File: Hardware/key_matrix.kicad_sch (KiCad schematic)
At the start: 80 parts, among them SW1 ESC, SW10 TAB, SW11 Q, SW12 W, SW13 E, SW14 R, SW15 T, SW16 NA, SW17 M1, SW18 CAPS, SW19 A, SW2 `, SW20 S, SW21 D, SW22 F, SW23 G, SW24 NA, SW25 M2, SW26 M3, SW28 SHIFT, SW29 CTRL, SW3 1, SW31 Z, SW32 WIN, SW34 X, SW35 FN, SW37 C, SW38 ALT, SW4 2, SW40 V, SW41 SPACE, SW43 B, SW44 DEL, SW46 NA, SW47 NA, SW5 3, SW6 4, SW7 5, SW8 6, SW9 M0

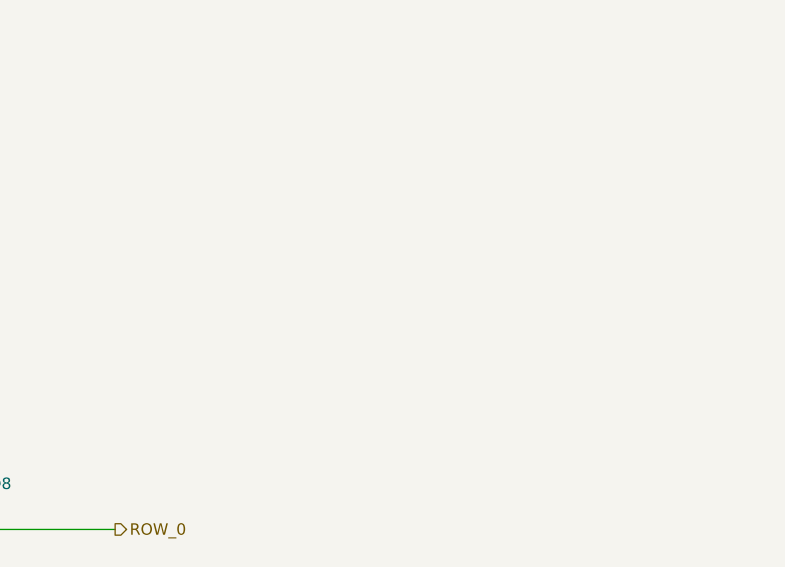
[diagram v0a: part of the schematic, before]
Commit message: added rotary encoder to schematic
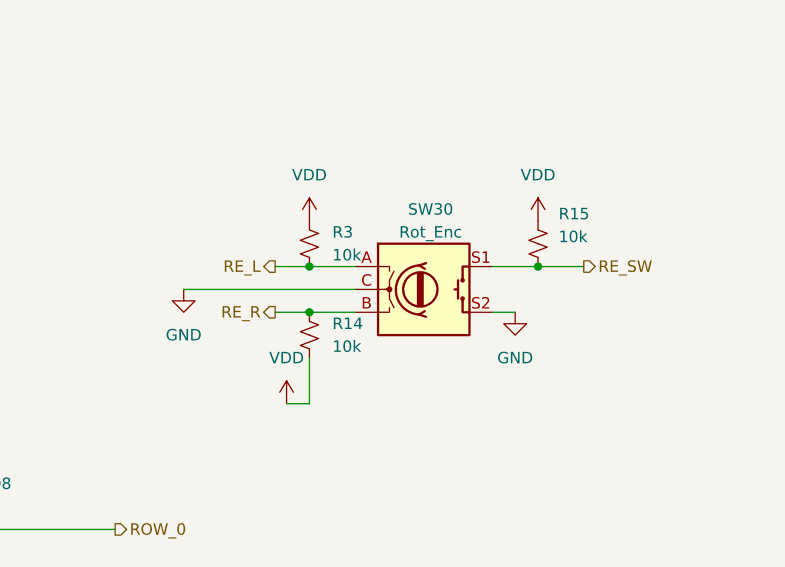
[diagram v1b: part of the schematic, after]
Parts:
- added R14, R15, R3: 10k, symbol Device:R_Small_US
- added SW30: Rot_Enc, symbol Device:RotaryEncoder_Switch
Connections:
- new net GND: SW30.C, SW30.S2
- new net RE_L: R3.1, SW30.A
- new net RE_R: R14.2, SW30.B
- new net RE_SW: R15.1, SW30.S1
- new net VDD: R14.1, R15.2, R3.2

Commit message: Update schematic for rotary encoder and matrix layout
Added new symbols and labels for rotary encoder connections, updated wire routing and junctions, and adjusted matrix row/column positions for improved clarity and alignment. Also corrected text annotations to better describe left and right hand keyboard sections.
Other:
- note added: "For the Left hand side (central) I want all letters and numbers (including B) Function rows F1-F6 esc TAB, CAPS, Shift Bottom row : ctrl,win,alt,spacebar (potential backspace) all key sizes found in a normal keycap set (except spacebar)"
- note added: "On the right hand side (Peripheral) we want the following keys: - All common right hand letters and numbers[7-0] (16) - Common punct. and typing function (space, enter, comma, etc) (16) - Arrow keys (4) - Function keys [7-12] (6) - Advanced Function [PU,PD,INS,DEL,HOME] (5) TOTAL ~47-50 keys RHS, ideally a 6x8 grid"
- note removed: "For the Left hand side (peripheral) I want all letters and numbers (including B) Function rows F1-F6 esc TAB, CAPS, Shift Bottom row : ctrl,win,alt,spacebar (potential backspace) all key sizes found in a normal keycap set (except spacebar)"
- note removed: "On the right hand side (central) we want the following keys: - All common right hand letters and numbers[7-0] (16) - Common punct. and typing function (space, enter, comma, etc) (16) - Arrow keys (4) - Function keys [7-12] (6) - Advanced Function [PU,PD,INS,DEL,HOME] (5) TOTAL ~47-50 keys RHS, ideally a 6x8 grid"
- moved on the sheet: D1, D10, D11, D12, D13, D14, D15, D16, D17, D18, D19, D2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

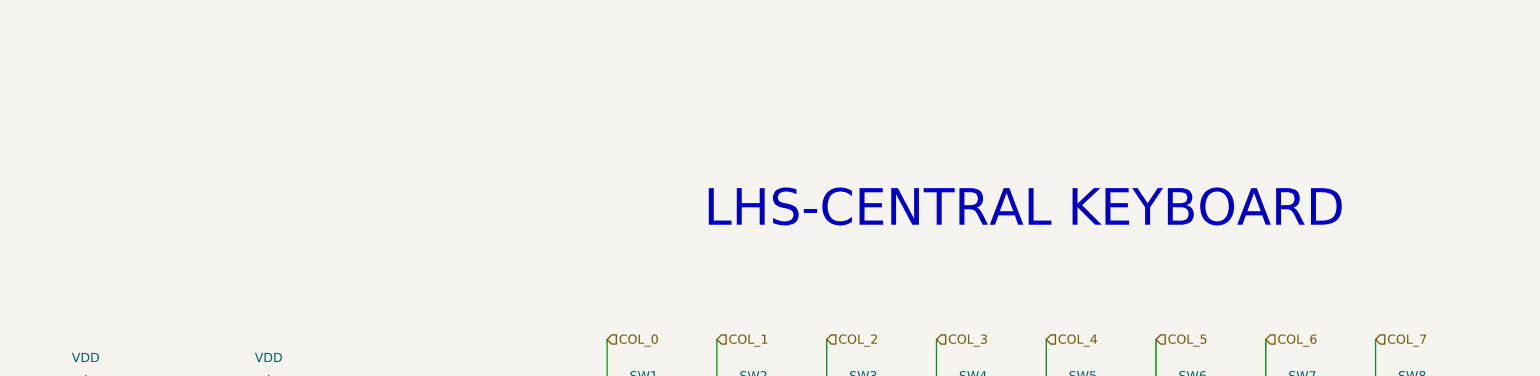
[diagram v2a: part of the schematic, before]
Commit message: Add antenna symbol and update schematic connections
Introduced a new Device:Antenna symbol to the hornet_kb schematic and added its instance. Updated various wire and junction connections, including changes to VBUS, GND, and capacitor placements. Replaced GND1 symbols with GND in power_management schematic for consistency. Adjusted text annotations and wire routing in all affected schematics to reflect new connections and improve clarity.
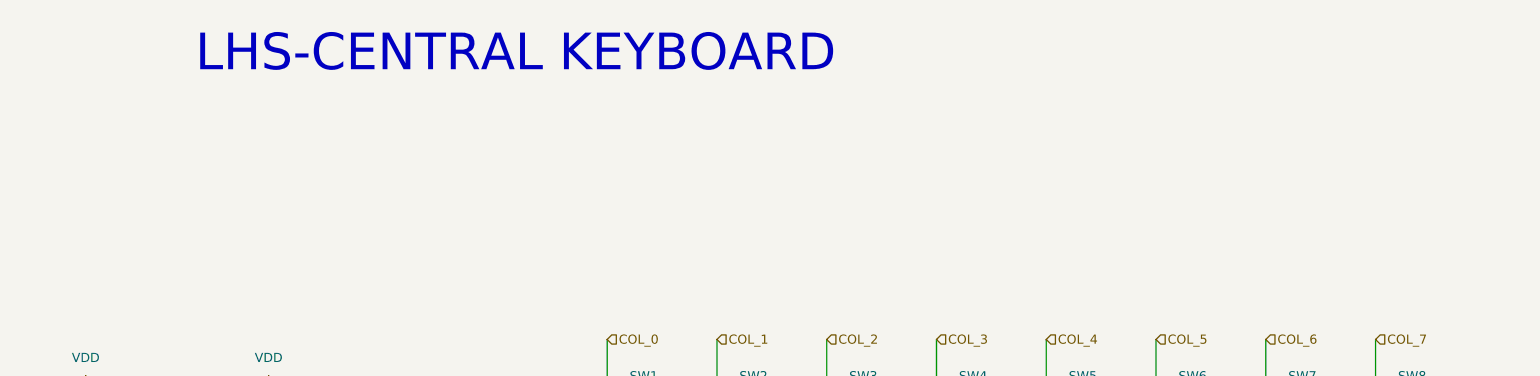
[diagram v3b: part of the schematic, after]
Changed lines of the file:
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@@
 	(text "LHS-CENTRAL KEYBOARD"
 		(exclude_from_sim no)
-		(at 282.702 55.626 0)
+		(at 212.09 34.036 0)
 		(effects
 			(font
